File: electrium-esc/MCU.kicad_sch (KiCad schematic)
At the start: 23 parts

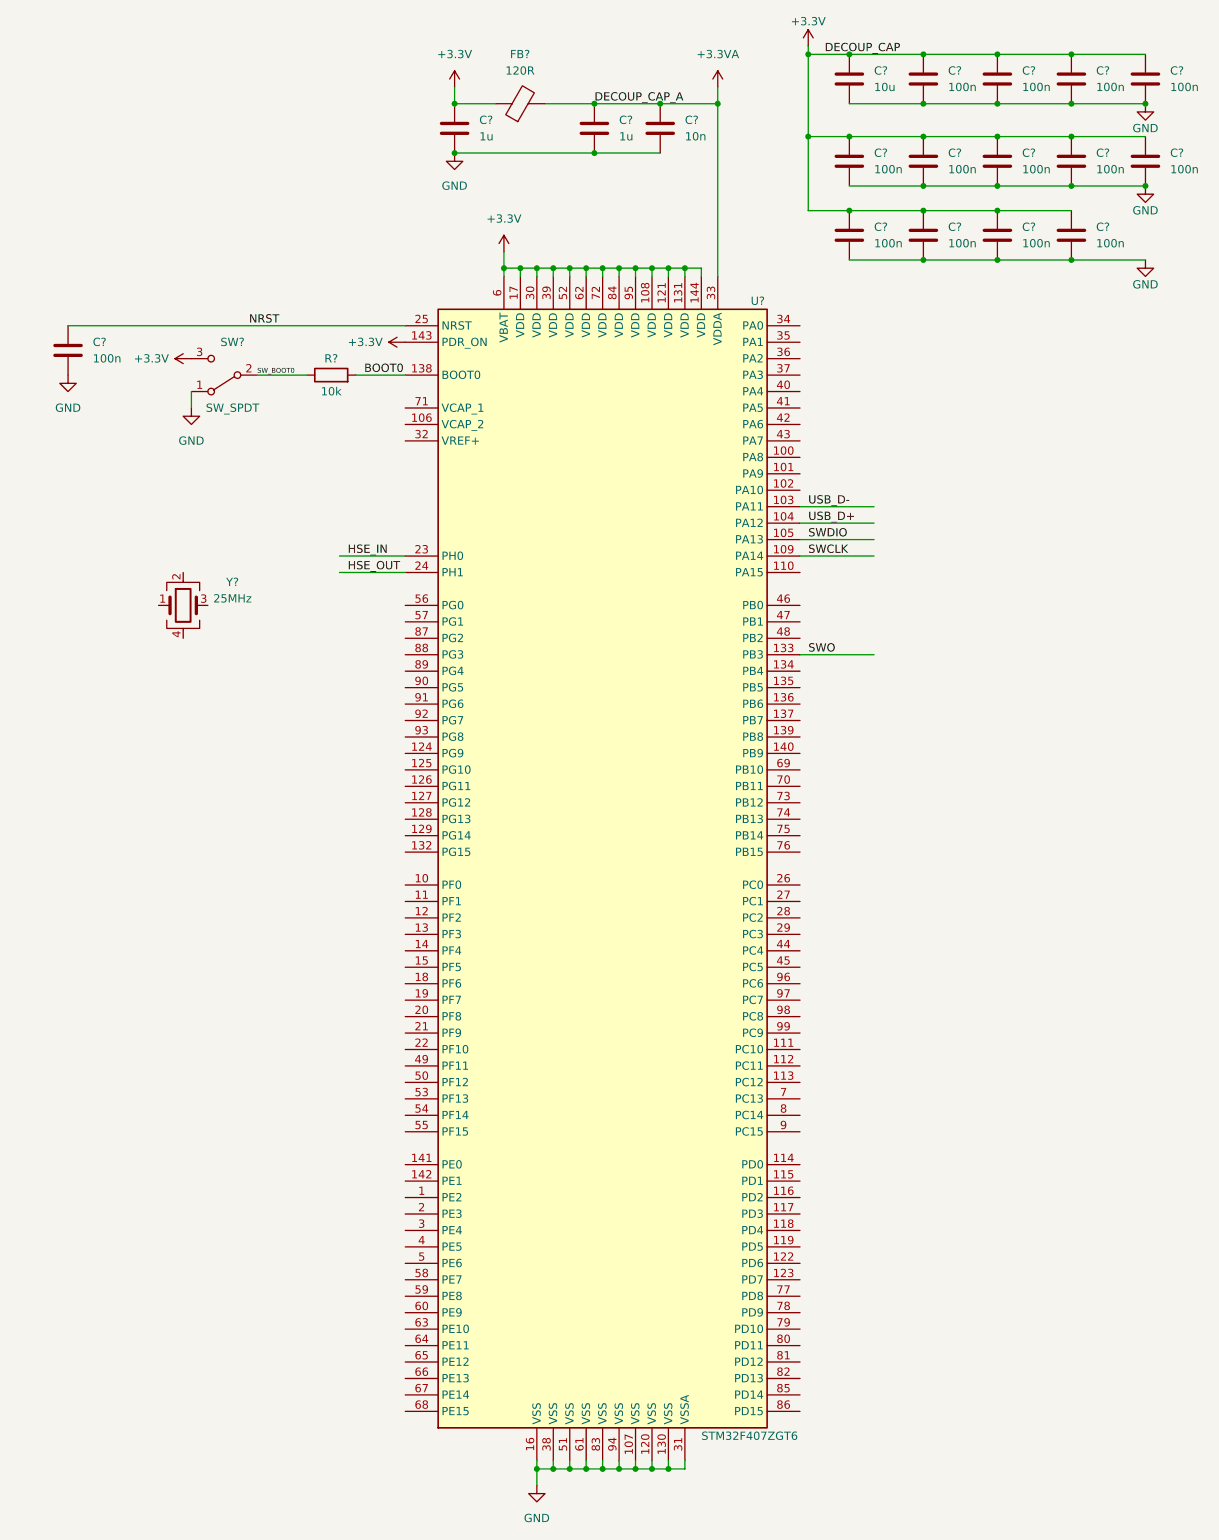
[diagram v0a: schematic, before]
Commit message: Complete Motor Driver!
Put in place passive components per documentation
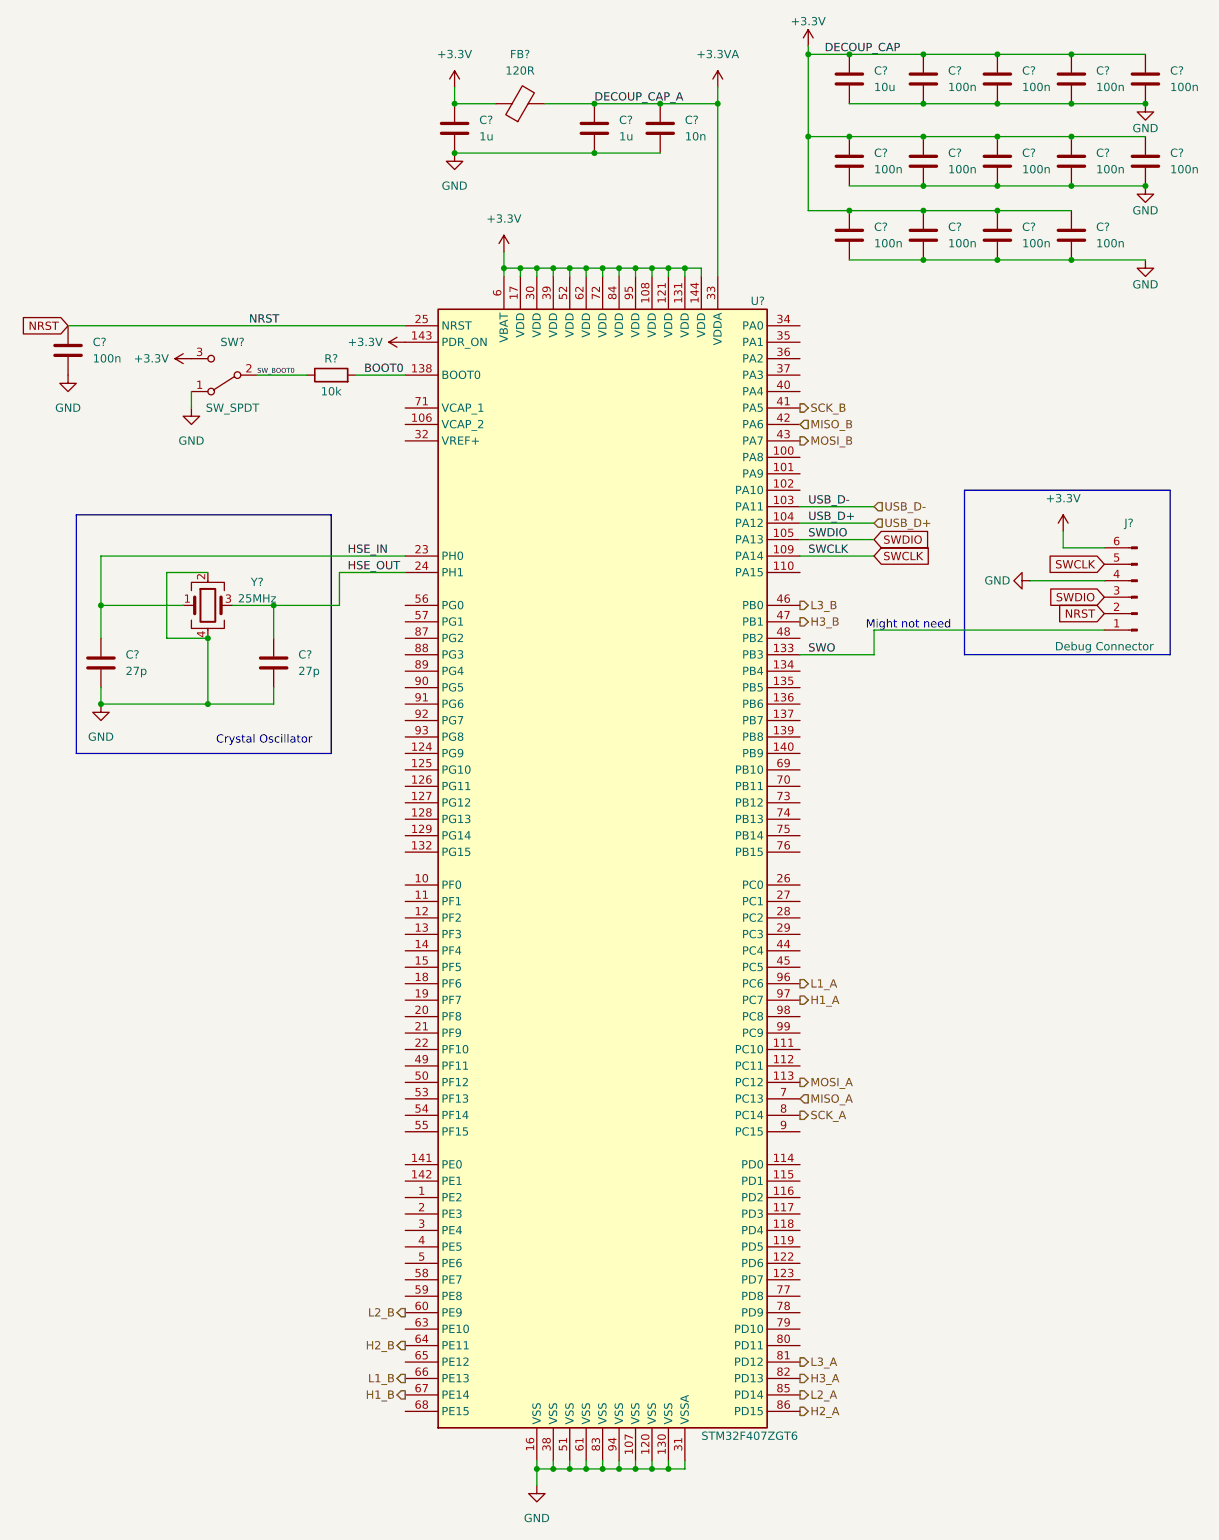
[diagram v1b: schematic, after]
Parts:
- added C? (x2): 27p, symbol Device:C
- added J?: Debug Connector, symbol Connector:Conn_01x06_Male
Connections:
- net +3.3V: now also J?.6 (Pin_6)
- net GND: now also Y?.2, Y?.4, C?.2, C?.2, J?.4 (Pin_4)
- net HSE_IN: now also Y?.1, C?.1
- net HSE_OUT: now also Y?.3, C?.1
- net NRST: now also J?.2 (Pin_2)
- net SWCLK: now also J?.5 (Pin_5)
- net SWDIO: now also J?.3 (Pin_3)
- net SWO: now also J?.1 (Pin_1)
- net MOSI_A: now reaches U?.113 (PC12)
- net SCK_B: now reaches U?.41 (PA5)
- net MISO_B: now reaches U?.42 (PA6)
- net MOSI_B: now reaches U?.43 (PA7)
- net L3_B: now reaches U?.46 (PB0)
- net H3_B: now reaches U?.47 (PB1)
- net L2_B: now reaches U?.60 (PE9)
- net H2_B: now reaches U?.64 (PE11)
- net L1_B: now reaches U?.66 (PE13)
- net H1_B: now reaches U?.67 (PE14)
- net MISO_A: now reaches U?.7 (PC13)
- net SCK_A: now reaches U?.8 (PC14)
- net L3_A: now reaches U?.81 (PD12)
- net H3_A: now reaches U?.82 (PD13)
- net L2_A: now reaches U?.85 (PD14)
- net H2_A: now reaches U?.86 (PD15)
- net L1_A: now reaches U?.96 (PC6)
- net H1_A: now reaches U?.97 (PC7)
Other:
- note added: "Crystal Oscillator"
- note added: "Might not need"
- moved on the sheet: Y?

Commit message: Add additional MCU connectivity
Still need to integrate NRF24L01 capabilities
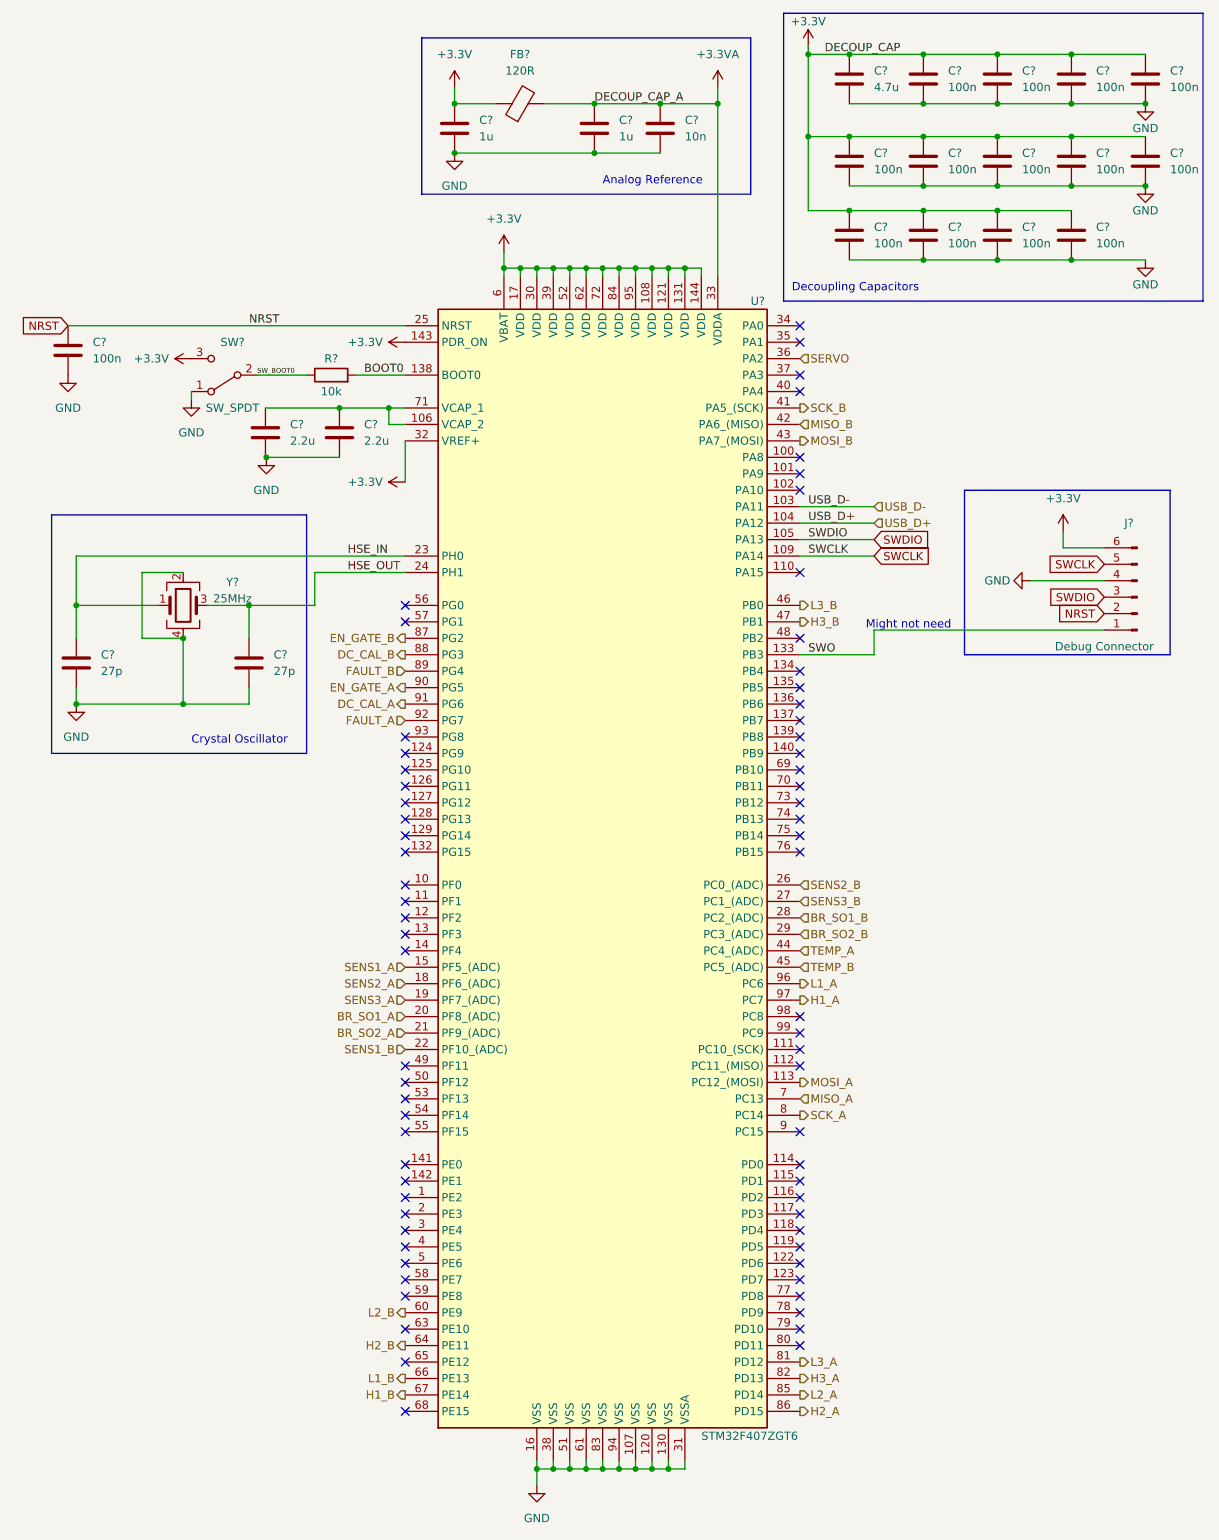
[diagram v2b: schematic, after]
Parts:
- added C? (x2): 2.2u, symbol Device:C
- C?: value 10u -> 4.7u
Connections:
- net +3.3V: now also U?.32 (VREF+)
- net GND: now also C?.2, C?.2
- net at U?.106 (VCAP_2): now also U?.71 (VCAP_1), C?.1, C?.1
- net SENS1_A: now reaches U?.15 (PF5_(ADC))
- net SENS2_A: now reaches U?.18 (PF6_(ADC))
- net SENS3_A: now reaches U?.19 (PF7_(ADC))
- net BR_SO1_A: now reaches U?.20 (PF8_(ADC))
- net BR_SO2_A: now reaches U?.21 (PF9_(ADC))
- net SENS1_B: now reaches U?.22 (PF10_(ADC))
- net SENS2_B: now reaches U?.26 (PC0_(ADC))
- net SENS3_B: now reaches U?.27 (PC1_(ADC))
- net BR_SO1_B: now reaches U?.28 (PC2_(ADC))
- net BR_SO2_B: now reaches U?.29 (PC3_(ADC))
- net SERVO: now reaches U?.36 (PA2)
- net TEMP_A: now reaches U?.44 (PC4_(ADC))
- net TEMP_B: now reaches U?.45 (PC5_(ADC))
- net EN_GATE_B: now reaches U?.87 (PG2)
- net DC_CAL_B: now reaches U?.88 (PG3)
- net FAULT_B: now reaches U?.89 (PG4)
- net EN_GATE_A: now reaches U?.90 (PG5)
- net DC_CAL_A: now reaches U?.91 (PG6)
- net FAULT_A: now reaches U?.92 (PG7)
- no-connect marks 0 -> 70
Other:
- note added: "Analog Reference"
- note added: "Decoupling Capacitors"
- moved on the sheet: C?, Y?

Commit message: Add additional connections to MCU
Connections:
- net MISO_A: now also U?.112 (PC11_(MISO)); no longer U?.7 (PC13)
- net SCK_A: now also U?.111 (PC10_(SCK)); no longer U?.8 (PC14)
- net CAN_RX: now reaches U?.114 (PD0)
- net CAN_TX: now reaches U?.115 (PD1)
- net GPIO1: now reaches U?.34 (PA0)
- net GPIO2: now reaches U?.35 (PA1)
- net NRF_SCK: now reaches U?.69 (PB10)
- net NRF_CSN: now reaches U?.73 (PB12)
- net NRF_CE: now reaches U?.74 (PB13)
- net NRF_MISO: now reaches U?.75 (PB14)
- net NRF_MOSI: now reaches U?.76 (PB15)
- no-connect marks 70 -> 61
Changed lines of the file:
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@@
   (junction (at 176.53 40.64) (diameter 0) (color 0 0 0 0)
   )
+  (no_connect (at 134.62 184.15))
+  (no_connect (at 134.62 181.61))
   (no_connect (at 73.66 196.85))
   (no_connect (at 73.66 135.89))
   (no_connect (at 134.62 115.57))
   (no_connect (at 73.66 107.95))
-  (no_connect (at 134.62 62.23))
   (no_connect (at 73.66 217.17))
-  (no_connect (at 134.62 130.81))
   (no_connect (at 134.62 133.35))
   (no_connect (at 73.66 105.41))
@@
   (no_connect (at 73.66 186.69))
   (no_connect (at 73.66 156.21))
-  (no_connect (at 134.62 173.99))
   (no_connect (at 134.62 100.33))
   (no_connect (at 134.62 186.69))
-  (no_connect (at 134.62 140.97))
   (no_connect (at 134.62 72.39))
   (no_connect (at 73.66 194.31))
-  (no_connect (at 134.62 138.43))
   (no_connect (at 134.62 196.85))
   (no_connect (at 73.66 181.61))
-  (no_connect (at 134.62 64.77))
   (no_connect (at 134.62 217.17))
   (no_connect (at 73.66 143.51))
   (no_connect (at 134.62 209.55))
   (no_connect (at 134.62 171.45))
-  (no_connect (at 134.62 176.53))
   (no_connect (at 134.62 207.01))
   (no_connect (at 73.66 140.97))
@@
   (no_connect (at 73.66 138.43))
   (no_connect (at 134.62 201.93))
-  (no_connect (at 134.62 143.51))
   (no_connect (at 134.62 125.73))
   (no_connect (at 73.66 184.15))
   (no_connect (at 73.66 176.53))
-  (no_connect (at 134.62 191.77))
   (no_connect (at 134.62 219.71))
   (no_connect (at 73.66 158.75))
@@
   (no_connect (at 134.62 82.55))
   (no_connect (at 134.62 87.63))
-  (no_connect (at 134.62 194.31))
-  (no_connect (at 134.62 135.89))
   (no_connect (at 134.62 69.85))
   (no_connect (at 73.66 128.27))
@@
     (effects (font (size 1.27 1.27)) (justify right))
   )
+  (hierarchical_label "NRF_CE" (shape output) (at 134.62 138.43 0)
+    (effects (font (size 1.27 1.27)) (justify left))
+  )
+  (hierarchical_label "GPIO1" (shape bidirectional) (at 134.62 62.23 0)
+    (effects (font (size 1.27 1.27)) (justify left))
+  )
+  (hierarchical_label "CAN_RX" (shape input) (at 134.62 191.77 0)
+    (effects (font (size 1.27 1.27)) (justify left))
+  )
   (hierarchical_label "FAULT_A" (shape input) (at 73.66 123.19 180)
     (effects (font (size 1.27 1.27)) (justify right))
@@
     (effects (font (size 1.27 1.27)) (justify right))
   )
-  (hierarchical_label "SCK_A" (shape output) (at 134.62 184.15 0)
+  (hierarchical_label "SCK_A" (shape output) (at 134.62 173.99 0)
     (effects (font (size 1.27 1.27)) (justify left))
   )
@@
     (effects (font (size 1.27 1.27)) (justify right))
   )
-  (hierarchical_label "MISO_A" (shape input) (at 134.62 181.61 0)
+  (hierarchical_label "MISO_A" (shape input) (at 134.62 176.53 0)
     (effects (font (size 1.27 1.27)) (justify left))
   )
@@
     (effects (font (size 1.27 1.27)) (justify right))
   )
+  (hierarchical_label "CAN_TX" (shape output) (at 134.62 194.31 0)
+    (effects (font (size 1.27 1.27)) (justify left))
+  )
   (hierarchical_label "FAULT_B" (shape input) (at 73.66 115.57 180)
     (effects (font (size 1.27 1.27)) (justify right))
@@
     (effects (font (size 1.27 1.27)) (justify left))
   )
+  (hierarchical_label "NRF_MISO" (shape input) (at 134.62 140.97 0)
+    (effects (font (size 1.27 1.27)) (justify left))
+  )
   (hierarchical_label "EN_GATE_B" (shape output) (at 73.66 110.49 180)
     (effects (font (size 1.27 1.27)) (justify right))
@@
     (effects (font (size 1.27 1.27)) (justify left))
   )
+  (hierarchical_label "NRF_CSN" (shape output) (at 134.62 135.89 0)
+    (effects (font (size 1.27 1.27)) (justify left))
+  )
   (hierarchical_label "SERVO" (shape input) (at 134.62 67.31 0)
     (effects (font (size 1.27 1.27)) (justify left))
@@
     (effects (font (size 1.27 1.27)) (justify left))
   )
+  (hierarchical_label "NRF_MOSI" (shape output) (at 134.62 143.51 0)
+    (effects (font (size 1.27 1.27)) (justify left))
+  )
   (hierarchical_label "L1_A" (shape output) (at 134.62 163.83 0)
     (effects (font (size 1.27 1.27)) (justify left))
   )
+  (hierarchical_label "GPIO2" (shape bidirectional) (at 134.62 64.77 0)
+    (effects (font (size 1.27 1.27)) (justify left))
+  )
   (hierarchical_label "DC_CAL_A" (shape output) (at 73.66 120.65 180)
     (effects (font (size 1.27 1.27)) (justify right))
@@
     (effects (font (size 1.27 1.27)) (justify left))
   )
+  (hierarchical_label "NRF_SCK" (shape output) (at 134.62 130.81 0)
+    (effects (font (size 1.27 1.27)) (justify left))
+  )

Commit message: Add additional connections to MCU
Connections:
- net AN_IN: now reaches U?.14 (PF4)
- no-connect marks 61 -> 60
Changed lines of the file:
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@@
   (no_connect (at 73.66 176.53))
   (no_connect (at 134.62 219.71))
-  (no_connect (at 73.66 158.75))
   (no_connect (at 134.62 123.19))
   (no_connect (at 73.66 130.81))
@@
     (effects (font (size 1.27 1.27)) (justify left))
   )
+  (hierarchical_label "AN_IN" (shape input) (at 73.66 158.75 180)
+    (effects (font (size 1.27 1.27)) (justify right))
+  )
   (hierarchical_label "GPIO1" (shape bidirectional) (at 134.62 62.23 0)
     (effects (font (size 1.27 1.27)) (justify left))
@@
     (effects (font (size 1.27 1.27)) (justify left))
   )
-  (hierarchical_label "SERVO" (shape input) (at 134.62 67.31 0)
-    (effects (font (size 1.27 1.27)) (justify left))
-  )
+  (hierarchical_label "SERVO" (shape output) (at 134.62 67.31 0)
+    (effects (font (size 1.27 1.27)) (justify left))
+  )

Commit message: Modify title
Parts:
- added C? (x2): 2.2u, symbol Device:C
- added PS?: TC2117-3.3VDBTR, SOT230P700X180-4N, symbol TC2117-3.3VDBTR:TC2117-3.3VDBTR
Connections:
- net +3.3V: now also C?.1, PS?.4 (VOUT_2)
- net GND: now also C?.1, C?.2, PS?.1 (GND)
- new net +5V: C?.2, PS?.3 (VIN)
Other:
- note added: "Voltage Regulator"
